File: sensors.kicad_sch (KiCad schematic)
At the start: 24 parts, among them U3 IIS2MDCTR, U4 LSM6DSO32TR, U5 TMP108AIYFFR, U6 LPS25HBTR, U8 OPT4001DTSR

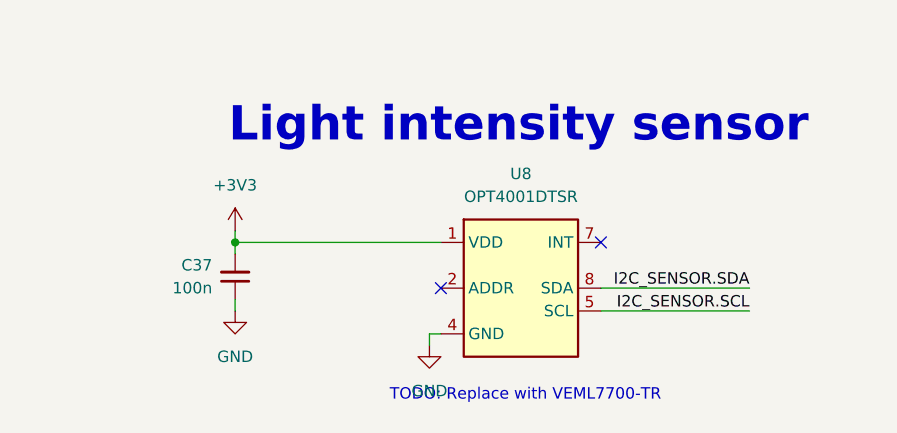
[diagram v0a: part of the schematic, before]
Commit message: [#95398] Initial component placement
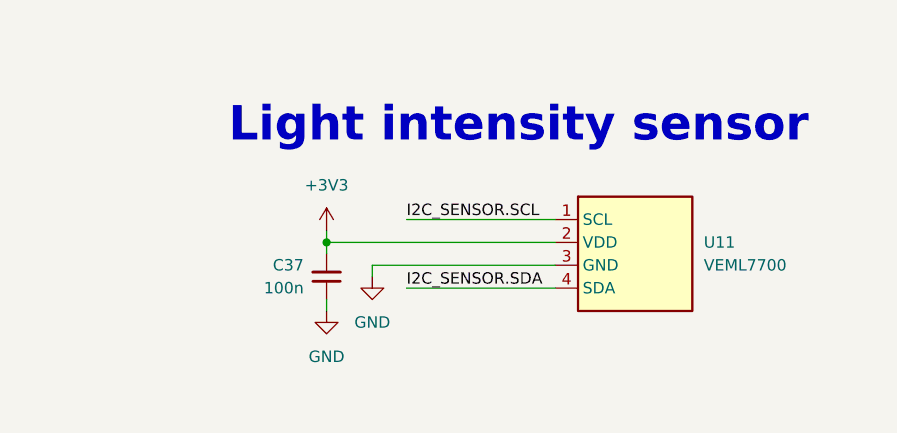
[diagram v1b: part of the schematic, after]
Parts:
- removed U8: OPT4001DTSR, antmicro-footprints:SOT-583, symbol antmicroOpticalSensorsAmbientLightIRUVSensors:OPT4001DTSR
- added U11: VEML7700, antmicro-footprints:VEML7700, symbol antmicroOpticalSensorsAmbientLightIRUVSensors:VEML7700
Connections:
- net +3V3: now also U11.2 (VDD)
- net GND: now also U11.3 (GND)
- net I2C_SENSOR.SCL: now also U11.1 (SCL)
- net I2C_SENSOR.SDA: now also U11.4 (SDA)
- no-connect marks 3 -> 1
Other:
- note removed: "TODO: Replace with VEML7700-TR"
- moved on the sheet: C37

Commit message: [#95398] Schematic cleanup
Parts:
- added R111, R139, R3, R47, R48, R49, R50, R6: R_0R_0402, antmicro-footprints:R_0402_1005Metric, symbol antmicroResistors0402:R_0R_0402
- U11: MPN VEML7700 -> VEML7700-TT
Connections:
- net I2C_SENSOR.SCL: now also R111.1, R3.2, R48.2, R49.1; no longer U11.1 (SCL), U4.13 (SCL), U5.B2 (SCL), U6.2 (SCL)
- net I2C_SENSOR.SDA: now also R139.1, R47.2, R50.1, R6.2; no longer U11.4 (SDA), U4.14 (SDA), U5.C2 (SDA), U6.4 (SDA)
- new net: R139.2, U11.4 (SDA)
- new net: R48.1, U6.2 (SCL)
- new net: R47.1, U6.4 (SDA)
- new net: R111.2, U11.1 (SCL)
- new net: R49.2, U5.B2 (SCL)
- new net: R50.2, U5.C2 (SDA)
- new net: R3.1, U4.13 (SCL)
- new net: R6.1, U4.14 (SDA)
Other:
- moved on the sheet: C37, C46, C47, C48, C49, C50, C51, C52, C53, C54, R104, R105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

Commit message: [#95398] Implement basic post review sugestions
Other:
- note added: "Addr 0x10"
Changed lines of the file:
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@@
+		)
+	)
+	(text "Addr 0x10"
+		(exclude_from_sim no)
+		(at 356.87 220.218 0)
+		(effects
+			(font
+				(size 1.27 1.27)
+			)
 		)
 	)

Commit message: [#95398] Add markings for ETH strap resistors
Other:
- title: renode-reference-platform -> STM32H7 Renode Reference Platform
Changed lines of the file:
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@@
 	(paper "A3")
 	(title_block
-		(title "renode-reference-platform")
+		(title "STM32H7 Renode Reference Platform")
 		(date "07.04.2026")
 		(rev "1.0.0")

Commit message: [#95451] Finalizing final placement
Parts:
- added TP20: TP_0.75mm_SMD, antmicro-footprints:TP_SMD_0.75mm, symbol antmicroTestPoints:TP_0.75mm_SMD
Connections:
- net at U5.C1 (~{ALERT}): now also TP20.1
- no-connect marks 1 -> 0
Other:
- moved on the sheet: R110, R47, R48
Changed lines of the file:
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@@
 		(color 0 0 0 0)
 	)
-	(no_connect
-		(at 233.68 212.09)
-	)
 	(bus_entry
 		(at 49.53 90.17)
@@
 	(wire
 		(pts
-			(xy 101.6 200.66) (xy 121.92 200.66)
+			(xy 102.87 200.66) (xy 121.92 200.66)
 		)
 		(stroke
@@
 	(wire
 		(pts
-			(xy 92.71 200.66) (xy 96.52 200.66)
+			(xy 92.71 200.66) (xy 97.79 200.66)
 		)
 		(stroke
@@
 	(wire
 		(pts
-			(xy 100.33 210.82) (xy 102.87 210.82)
+			(xy 102.87 210.82) (xy 107.95 210.82)
 		)
 		(stroke
@@
 	(wire
 		(pts
+			(xy 234.95 212.09) (xy 233.68 212.09)
+		)
+		(stroke
+			(width 0)
+			(type default)
+		)
+	)
+	(wire
+		(pts
 			(xy 125.73 80.01) (xy 125.73 82.55)
 		)
@@
 	(wire
 		(pts
-			(xy 101.6 203.2) (xy 121.92 203.2)
+			(xy 102.87 203.2) (xy 121.92 203.2)
 		)
 		(stroke
@@
 	(wire
 		(pts
-			(xy 92.71 203.2) (xy 96.52 203.2)
+			(xy 92.71 203.2) (xy 97.79 203.2)
 		)
 		(stroke
@@
 	(wire
 		(pts
-			(xy 92.71 210.82) (xy 95.25 210.82)
+			(xy 92.71 210.82) (xy 97.79 210.82)
 		)
 		(stroke
@@
 	(hierarchical_label "BAR_~{INT}"
 		(shape output)
-		(at 102.87 210.82 0)
+		(at 107.95 210.82 0)
 		(effects
 			(font
@@
 	(symbol
 		(lib_id "antmicroResistors0402:R_0R_0402")
-		(at 96.52 203.2 0)
+		(at 97.79 203.2 0)
 		(unit 1)
 		(exclude_from_sim no)
@@
 		(dnp no)
 		(property "Reference" "R48"
-			(at 94.234 202.184 0)
+			(at 95.504 202.184 0)
 			(effects
 				(font
@@
 		)
 		(property "Value" "R_0R_0402"
-			(at 116.84 215.9 0)
+			(at 118.11 215.9 0)
 			(effects
 				(font
@@
 		)
 		(property "Footprint" "antmicro-footprints:R_0402_1005Metric"
-			(at 116.84 218.44 0)
+			(at 118.11 218.44 0)
 			(effects
 				(font
@@
 		)
 		(property "Datasheet" "https://industrial.panasonic.com/cdbs/www-data/pdf/RDA0000/AOA0000C301.pdf"
-			(at 116.84 220.98 0)
+			(at 118.11 220.98 0)
 			(effects
 				(font
@@
 		)
 		(property "Description" "SMD Chip Resistor, Jumper, 0 ohm, 100 mW, 0402 [1005 Metric], Thick Film, General Purpose"
-			(at 116.84 236.22 0)
+			(at 118.11 236.22 0)
 			(effects
 				(font
@@
 		)
 		(property "MPN" "ERJ2GE0R00X"
-			(at 116.84 223.52 0)
+			(at 118.11 223.52 0)
 			(effects
 				(font
@@
 		)
 		(property "Manufacturer" "Panasonic"
-			(at 116.84 226.06 0)
+			(at 118.11 226.06 0)
 			(effects
 				(font
@@
 		)
 		(property "License" "Apache-2.0"
-			(at 116.84 228.6 0)
+			(at 118.11 228.6 0)
 			(effects
 				(font
@@
 		)
 		(property "Author" "Antmicro"
-			(at 116.84 231.14 0)
+			(at 118.11 231.14 0)
 			(effects
 				(font
@@
 		)
 		(property "Val" "0R"
-			(at 103.124 202.184 0)
+			(at 104.394 202.184 0)
 			(effects
 				(font
@@
 		)
 		(property "Tolerance" "~"
-			(at 116.84 213.36 0)
+			(at 118.11 213.36 0)
 			(effects
 				(font
@@
 		)
 		(property "Current" "1A"
-			(at 116.84 233.68 0)
+			(at 118.11 233.68 0)
 			(effects
 				(font
@@
 	)
 	(symbol
+		(lib_id "antmicroTestPoints:TP_0.75mm_SMD")
+		(at 234.95 212.09 0)
+		(unit 1)
+		(exclude_from_sim no)
+		(in_bom no)
+		(on_board yes)
+		(dnp no)
+		(fields_autoplaced yes)
+		(property "Reference" "TP20"
+			(at 240.03 212.09 0)
+			(effects
+				(font
+					(size 1.27 1.27)
+					(thickness 0.15)
+				)
+				(justify left)
+			)
+		)
+		(property "Value" "TP_0.75mm_SMD"
+			(at 245.11 215.9 0)
+			(effects
+				(font
+					(size 1.27 1.27)
+					(thickness 0.15)
+				)
+				(justify left bottom)
+				(hide yes)
+			)
+		)
+		(property "Footprint" "antmicro-footprints:TP_SMD_0.75mm"
+			(at 245.11 218.44 0)
+			(effects
+				(font
+					(size 1.27 1.27)
+					(thickness 0.15)
+				)
+				(justify left bottom)
+				(hide yes)
+			)
+		)
+		(property "Datasheet" ""
+			(at 252.73 224.79 0)
+			(effects
+				(font
+					(size 1.27 1.27)
+					(thickness 0.15)
+				)
+				(justify left bottom)
+				(hide yes)
+			)
+		)
+		(property "Description" "SMT test point"
+			(at 245.745 226.06 0)
+			(effects
+				(font
+					(size 1.27 1.27)
+				)
+				(justify left bottom)
+				(hide yes)
+			)
+		)
+		(property "MPN" ""
+			(at 245.745 223.52 0)
+			(effects
+				(font
+					(size 1.27 1.27)
+					(thickness 0.15)
+				)
+				(justify left bottom)
+				(hide yes)
+			)
+		)
+		(property "Manufacturer" ""
+			(at 245.745 218.44 0)
+			(effects
+				(font
+					(size 1.27 1.27)
+					(thickness 0.15)
+				)
+				(justify left bottom)
+				(hide yes)
+			)
+		)
+		(property "Author" "Antmicro"
+			(at 245.11 220.98 0)
+			(effects
+				(font
+					(size 1.27 1.27)
+					(thickness 0.15)
+				)
+				(justify left bottom)
+				(hide yes)
+			)
+		)
+		(property "License" "Apache-2.0"
+			(at 245.11 223.52 0)
+			(effects
+				(font
+					(size 1.27 1.27)
+					(thickness 0.15)
+				)
+				(justify left bottom)
+				(hide yes)
+			)
+		)
+		(pin "1"
+		)
+		(instances
+			(project "renode-reference-platform"
+				(path "/126ae87b-f292-4372-94ff-ae46971d67ab/143ac980-6d59-4a8b-9ea3-64cd140d4a49"
+					(reference "TP20")
+					(unit 1)
+				)
+			)
+		)
+	)
+	(symbol
 		(lib_id "antmicroResistors0402:R_0R_0402")
 		(at 130.81 95.25 0)
@@
 	(symbol
 		(lib_id "antmicroResistors0402:R_0R_0402")
-		(at 96.52 200.66 0)
+		(at 97.79 200.66 0)
 		(unit 1)
 		(exclude_from_sim no)
@@
 		(dnp no)
 		(property "Reference" "R47"
-			(at 94.234 199.644 0)
+			(at 95.504 199.644 0)
 			(effects
 				(font
@@
 		)
 		(property "Value" "R_0R_0402"
-			(at 116.84 213.36 0)
+			(at 118.11 213.36 0)
 			(effects
 				(font
@@
 		)
 		(property "Footprint" "antmicro-footprints:R_0402_1005Metric"
-			(at 116.84 215.9 0)
+			(at 118.11 215.9 0)
 			(effects
 				(font
@@
 		)
 		(property "Datasheet" "https://industrial.panasonic.com/cdbs/www-data/pdf/RDA0000/AOA0000C301.pdf"
-			(at 116.84 218.44 0)
+			(at 118.11 218.44 0)
 			(effects
 				(font
@@
 		)
 		(property "Description" "SMD Chip Resistor, Jumper, 0 ohm, 100 mW, 0402 [1005 Metric], Thick Film, General Purpose"
-			(at 116.84 233.68 0)
+			(at 118.11 233.68 0)
 			(effects
 				(font
@@
 		)
 		(property "MPN" "ERJ2GE0R00X"
-			(at 116.84 220.98 0)
+			(at 118.11 220.98 0)
 			(effects
 				(font
@@
 		)
 		(property "Manufacturer" "Panasonic"
-			(at 116.84 223.52 0)
+			(at 118.11 223.52 0)
 			(effects
 				(font
@@
 		)
 		(property "License" "Apache-2.0"
-			(at 116.84 226.06 0)
+			(at 118.11 226.06 0)
 			(effects
 				(font
@@
 		)
 		(property "Author" "Antmicro"
-			(at 116.84 228.6 0)
+			(at 118.11 228.6 0)
 			(effects
 				(font
@@
 		)
 		(property "Val" "0R"
-			(at 103.124 199.644 0)
+			(at 104.394 199.644 0)
 			(effects
 				(font
@@
 		)
 		(property "Tolerance" "~"
-			(at 116.84 210.82 0)
+			(at 118.11 210.82 0)
 			(effects
 				(font
@@
 		)
 		(property "Current" "1A"
-			(at 116.84 231.14 0)
+			(at 118.11 231.14 0)
 			(effects
 				(font
@@
 	(symbol
 		(lib_id "antmicroResistors0402:R_0R_0402")
-		(at 95.25 210.82 0)
+		(at 97.79 210.82 0)
 		(unit 1)
 		(exclude_from_sim no)
@@
 		(dnp no)
 		(property "Reference" "R110"
-			(at 97.79 207.01 0)
+			(at 95.25 209.55 0)
 			(effects
 				(font
@@
 		)
 		(property "Value" "R_0R_0402"
-			(at 115.57 223.52 0)
+			(at 118.11 223.52 0)
 			(effects
 				(font
@@
 		)
 		(property "Footprint" "antmicro-footprints:R_0402_1005Metric"
-			(at 115.57 226.06 0)
+			(at 118.11 226.06 0)
 			(effects
 				(font
@@
 		)
 		(property "Datasheet" "https://industrial.panasonic.com/cdbs/www-data/pdf/RDA0000/AOA0000C301.pdf"
-			(at 115.57 228.6 0)
+			(at 118.11 228.6 0)
 			(effects
 				(font
@@
 		)
 		(property "Description" "SMD Chip Resistor, Jumper, 0 ohm, 100 mW, 0402 [1005 Metric], Thick Film, General Purpose"
-			(at 115.57 243.84 0)
+			(at 118.11 243.84 0)
 			(effects
 				(font
@@
 		)
 		(property "MPN" "ERJ2GE0R00X"
-			(at 115.57 231.14 0)
+			(at 118.11 231.14 0)
 			(effects
 				(font
@@
 		)
 		(property "Manufacturer" "Panasonic"
-			(at 115.57 233.68 0)
+			(at 118.11 233.68 0)
 			(effects
 				(font
@@
 		)
 		(property "License" "Apache-2.0"
-			(at 115.57 236.22 0)
+			(at 118.11 236.22 0)
 			(effects
 				(font
@@
 		)
 		(property "Author" "Antmicro"
-			(at 115.57 238.76 0)
+			(at 118.11 238.76 0)
 			(effects
 				(font
@@
 		)
 		(property "Val" "0R"
-			(at 97.79 208.788 0)
+			(at 104.14 209.55 0)
 			(effects
 				(font
@@
 		)
 		(property "Tolerance" "~"
-			(at 115.57 220.98 0)
+			(at 118.11 220.98 0)
 			(effects
 				(font
@@
 		)
 		(property "Current" "1A"
-			(at 115.57 241.3 0)
+			(at 118.11 241.3 0)
 			(effects
 				(font
